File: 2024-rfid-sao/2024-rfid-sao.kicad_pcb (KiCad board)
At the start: 2 copper layers, 60 x 119.4 mm, 10 parts, among them U1 M24LR64E, X1 Badgelife_sao_connector_v169b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

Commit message: 2024-rfid-sao: updates for jlcpcb
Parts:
- added REF**: JLC_TOOL_HOLE, library:JLC_TOOL_HOLE, F.Cu at (134.8, 170.0)
- added REF**: JLC_TOOL_HOLE, library:JLC_TOOL_HOLE, F.Cu at (73.7, 110.9)
- moved X1 36.5 mm to (133.8, 171.0), turned to -45 degrees
- moved G*** 28.5 mm to (73.7, 110.9), turned to 45 degrees
- moved L1 28.5 mm to (73.7, 110.9), turned to 0 degrees
- moved TP1 12.1 mm to (84.3, 135.7), turned to -135 degrees
- moved TP2 12.1 mm to (98.4, 121.5), turned to -135 degrees
- moved R2 11.5 mm to (95.6, 122.9), turned to -45 degrees
- moved R1 10.8 mm to (94.2, 124.3), turned to -45 degrees
- moved U1 9.38 mm to (91.3, 128.6), turned to -45 degrees
- moved C1 9.24 mm to (88.4, 134.1), turned to 135 degrees
- moved C2 8.42 mm to (89.9, 132.8), turned to 135 degrees
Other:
- board size 60 x 119.4 mm -> 95.8 x 95.8 mm

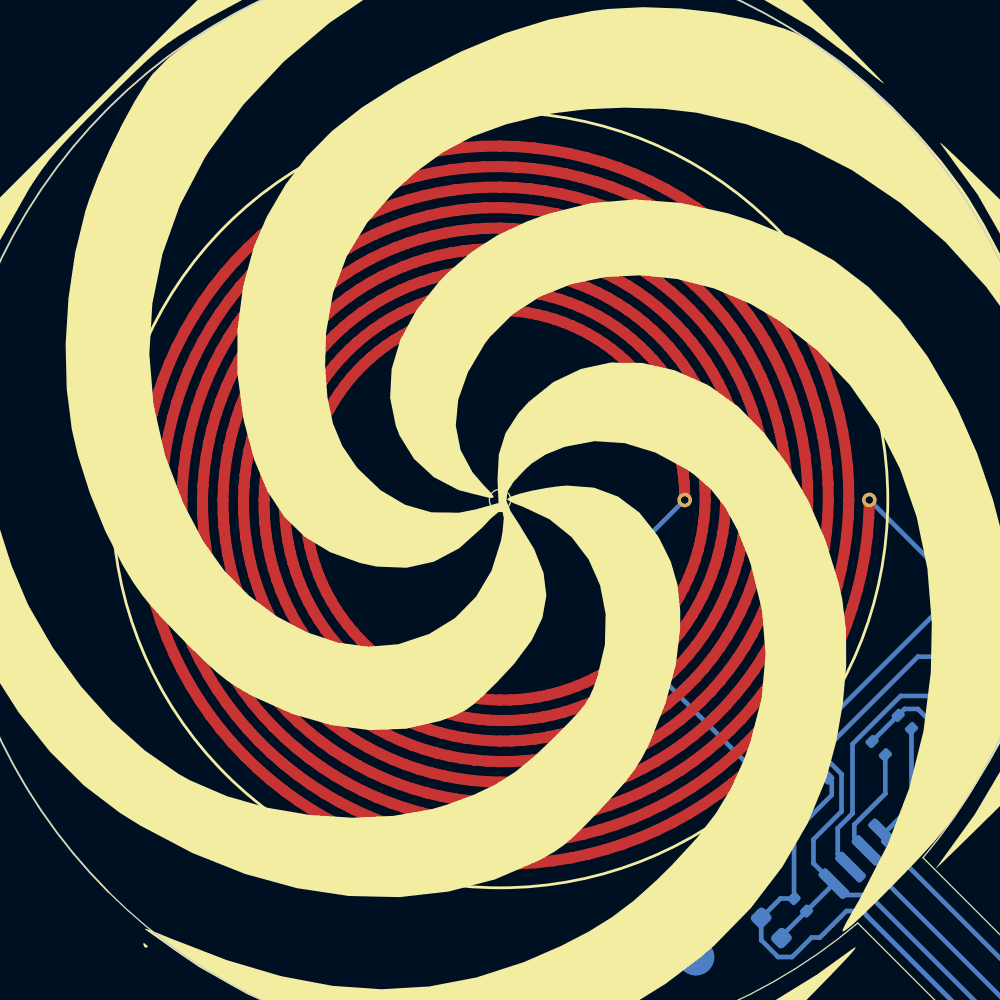
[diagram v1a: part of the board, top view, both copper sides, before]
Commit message: 2024-rfid-sao:remove from silk circle from antenna
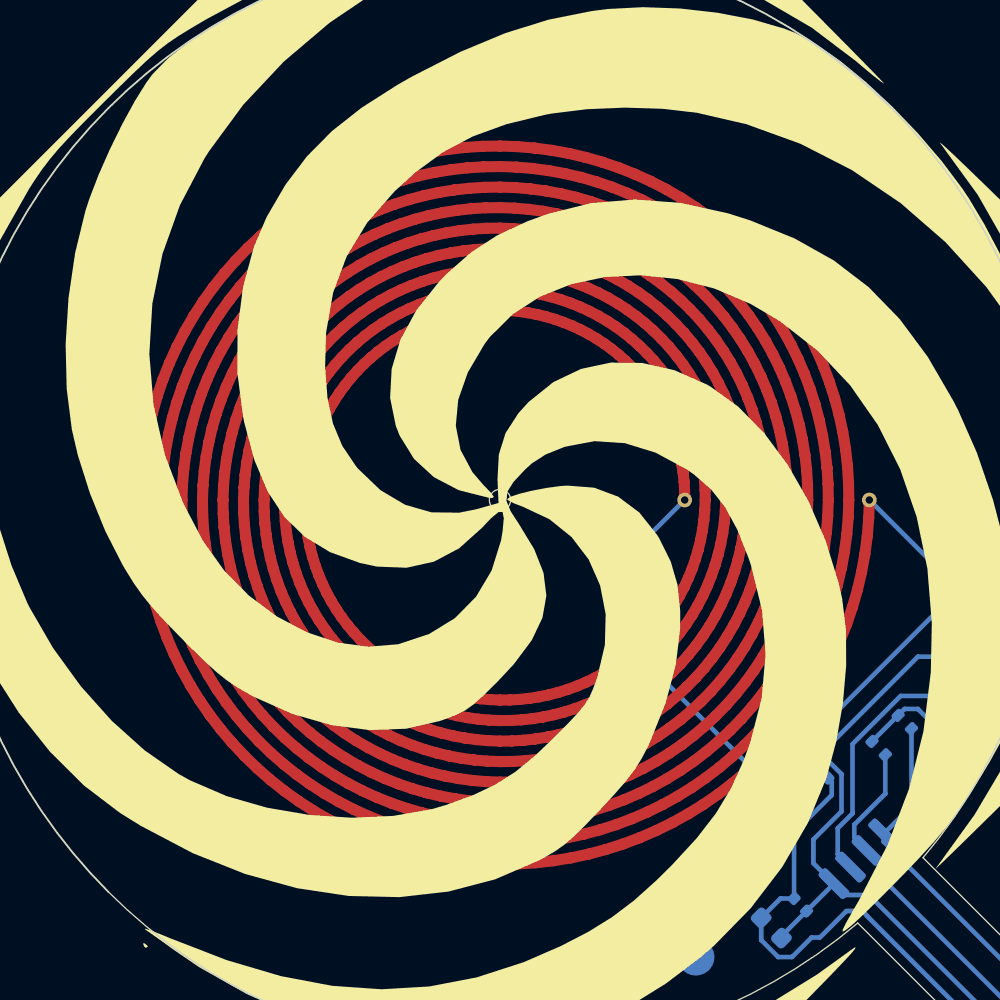
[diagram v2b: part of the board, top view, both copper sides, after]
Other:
- board text added: "@TomKeddie RFID-SAO Oct2024"
- board text removed: "@TomKeddie RFID-SAO Sept2024"

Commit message: 2024-rfid-sao: ready for second run
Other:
- board text added: "@TomKeddie RFID-SAO Nov2024 i2c: 0x53/0x57"
- board text removed: "@TomKeddie RFID-SAO Oct2024"
- board text removed: "JLCJLCJLCJLC"
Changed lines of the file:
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@@
 		(layer "Edge.Cuts")
 	)
-	(gr_text "@TomKeddie\nRFID-SAO\nOct2024"
+	(gr_text "@TomKeddie\nRFID-SAO\nNov2024\ni2c: 0x53/0x57"
 		(at 73.660272 110.910272 45)
 		(layer "B.SilkS")
@@
 			)
 			(justify mirror)
-		)
-	)
-	(gr_text "JLCJLCJLCJLC"
-		(at 113.965359 151.215359 -45)
-		(layer "B.SilkS")
-		(effects
-			(font
-				(size 2 2)
-				(thickness 0.3)
-			)
-			(justify mirror)
